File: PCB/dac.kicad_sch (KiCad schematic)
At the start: 8 parts, among them U4 DACx3202

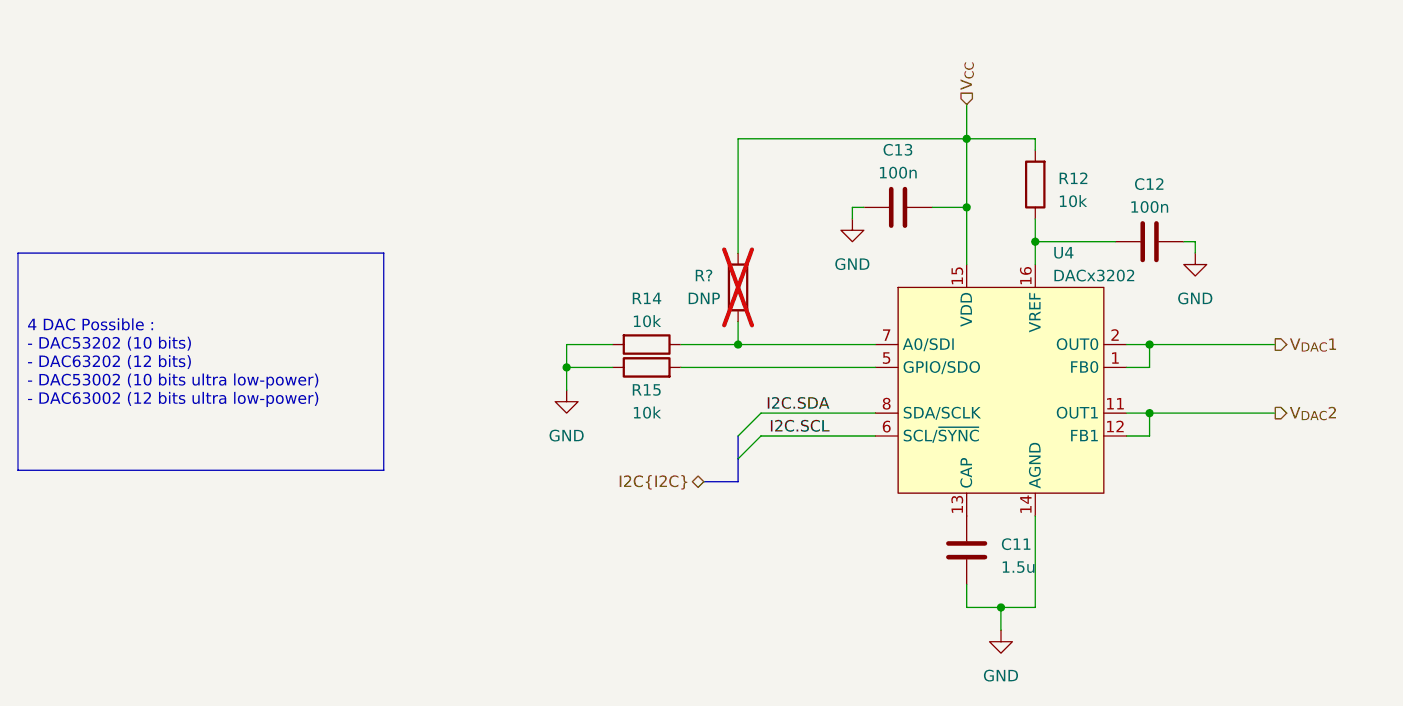
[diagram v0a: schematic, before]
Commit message: done with sch before ERC and footprints
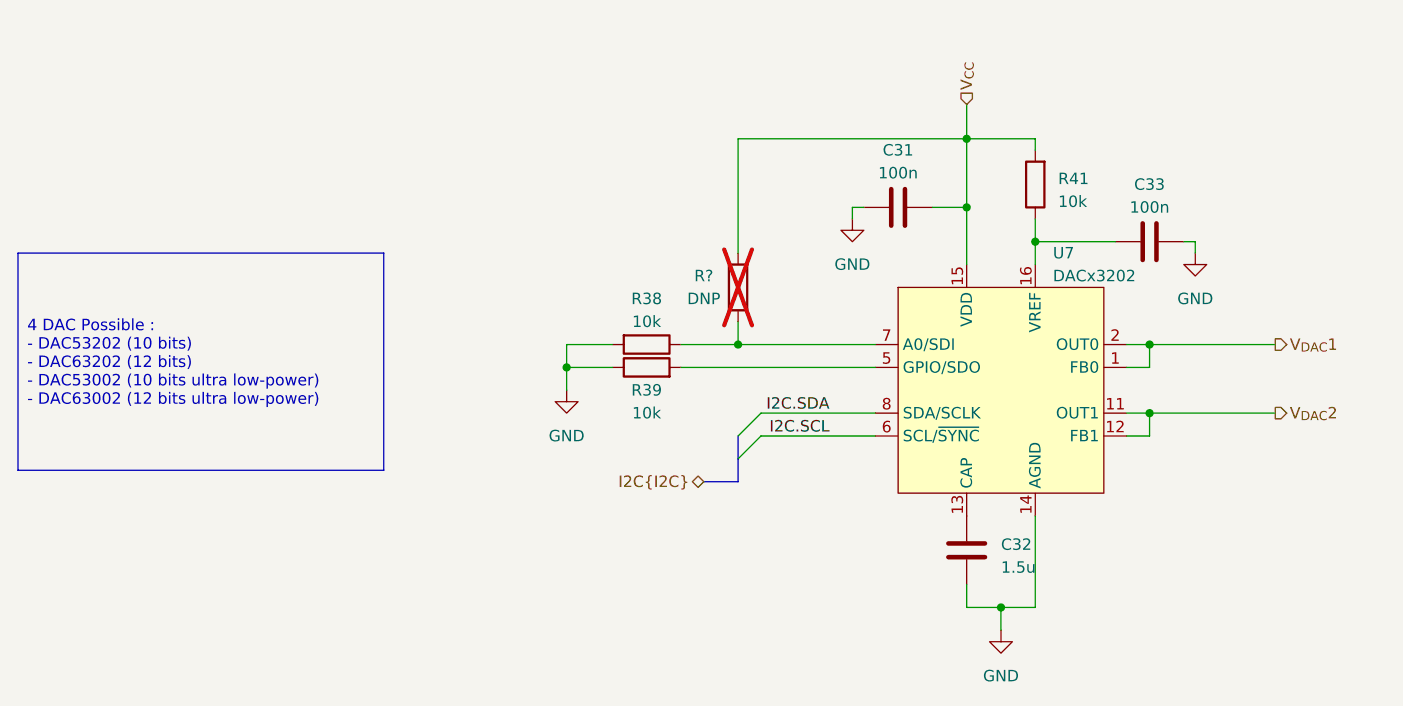
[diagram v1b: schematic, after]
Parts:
- renumbered C13 to C31, C11 to C32, C12 to C33, R14 to R38, R15 to R39, R12 to R41, U4 to U7
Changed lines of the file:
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@@
     (effects (font (size 1.27 1.27)) (justify left))
   )
-  (label "I2C.SCL" (at 134.62 110.49 180)
+  (label "I2C.SCL" (at 134.62 110.49 180) (fields_autoplaced)
     (effects (font (size 1.27 1.27)) (justify right bottom))
   )
-  (label "I2C.SDA" (at 134.62 107.95 180)
+  (label "I2C.SDA" (at 134.62 107.95 180) (fields_autoplaced)
     (effects (font (size 1.27 1.27)) (justify right bottom))
   )
@@
   (symbol (lib_id "power:GND") (at 137.16 86.36 0) (unit 1)
     (in_bom yes) (on_board yes) (dnp no) (fields_autoplaced)
-    (property "Reference" "#PWR031" (at 137.16 92.71 0)
+    (property "Reference" "#PWR065" (at 137.16 92.71 0)
       (effects (font (size 1.27 1.27)) hide)
     )
@@
       (project "Tattoo_Supply"
         (path "/036b57f3-323c-4da7-bad2-1c27fa1415e1/9f555ace-da32-4118-b59a-cfcb78baf4ed"
-          (reference "#PWR031") (unit 1)
+          (reference "#PWR065") (unit 1)
         )
       )
@@
   (symbol (lib_id "Device:R") (at 114.3 102.87 90) (unit 1)
     (in_bom yes) (on_board yes) (dnp no)
-    (property "Reference" "R15" (at 114.3 105.41 90)
+    (property "Reference" "R39" (at 114.3 105.41 90)
       (effects (font (size 1.27 1.27)))
     )
@@
       (project "Tattoo_Supply"
         (path "/036b57f3-323c-4da7-bad2-1c27fa1415e1/9f555ace-da32-4118-b59a-cfcb78baf4ed"
-          (reference "R15") (unit 1)
+          (reference "R39") (unit 1)
         )
       )
@@
         )
         (path "/036b57f3-323c-4da7-bad2-1c27fa1415e1/9f555ace-da32-4118-b59a-cfcb78baf4ed"
-          (reference "R13") (unit 1)
+          (reference "R40") (unit 1)
         )
       )
@@
   (symbol (lib_id "Device:R") (at 114.3 100.33 270) (unit 1)
     (in_bom yes) (on_board yes) (dnp no) (fields_autoplaced)
-    (property "Reference" "R14" (at 114.3 95.25 90)
+    (property "Reference" "R38" (at 114.3 95.25 90)
       (effects (font (size 1.27 1.27)))
     )
@@
       (project "Tattoo_Supply"
         (path "/036b57f3-323c-4da7-bad2-1c27fa1415e1/9f555ace-da32-4118-b59a-cfcb78baf4ed"
-          (reference "R14") (unit 1)
+          (reference "R38") (unit 1)
         )
       )
@@
   (symbol (lib_id "Device:C") (at 142.24 85.09 90) (unit 1)
     (in_bom yes) (on_board yes) (dnp no) (fields_autoplaced)
-    (property "Reference" "C13" (at 142.24 78.74 90)
+    (property "Reference" "C31" (at 142.24 78.74 90)
       (effects (font (size 1.27 1.27)))
     )
@@
       (project "Tattoo_Supply"
         (path "/036b57f3-323c-4da7-bad2-1c27fa1415e1/9f555ace-da32-4118-b59a-cfcb78baf4ed"
-          (reference "C13") (unit 1)
+          (reference "C31") (unit 1)
         )
       )
@@
   (symbol (lib_id "power:GND") (at 105.41 105.41 0) (unit 1)
     (in_bom yes) (on_board yes) (dnp no) (fields_autoplaced)
-    (property "Reference" "#PWR032" (at 105.41 111.76 0)
+    (property "Reference" "#PWR064" (at 105.41 111.76 0)
       (effects (font (size 1.27 1.27)) hide)
     )
@@
       (project "Tattoo_Supply"
         (path "/036b57f3-323c-4da7-bad2-1c27fa1415e1/9f555ace-da32-4118-b59a-cfcb78baf4ed"
-          (reference "#PWR032") (unit 1)
+          (reference "#PWR064") (unit 1)
         )
       )
@@
   (symbol (lib_id "Device:C") (at 149.86 123.19 0) (unit 1)
     (in_bom yes) (on_board yes) (dnp no) (fields_autoplaced)
-    (property "Reference" "C11" (at 153.67 122.555 0)
+    (property "Reference" "C32" (at 153.67 122.555 0)
       (effects (font (size 1.27 1.27)) (justify left))
     )
@@
       (project "Tattoo_Supply"
         (path "/036b57f3-323c-4da7-bad2-1c27fa1415e1/9f555ace-da32-4118-b59a-cfcb78baf4ed"
-          (reference "C11") (unit 1)
+          (reference "C32") (unit 1)
         )
       )
@@
   (symbol (lib_id "power:GND") (at 175.26 90.17 0) (unit 1)
     (in_bom yes) (on_board yes) (dnp no) (fields_autoplaced)
-    (property "Reference" "#PWR030" (at 175.26 96.52 0)
+    (property "Reference" "#PWR067" (at 175.26 96.52 0)
       (effects (font (size 1.27 1.27)) hide)
     )
@@
       (project "Tattoo_Supply"
         (path "/036b57f3-323c-4da7-bad2-1c27fa1415e1/9f555ace-da32-4118-b59a-cfcb78baf4ed"
-          (reference "#PWR030") (unit 1)
+          (reference "#PWR067") (unit 1)
         )
       )
@@
   (symbol (lib_id "Device:R") (at 157.48 82.55 180) (unit 1)
     (in_bom yes) (on_board yes) (dnp no) (fields_autoplaced)
-    (property "Reference" "R12" (at 160.02 81.915 0)
+    (property "Reference" "R41" (at 160.02 81.915 0)
       (effects (font (size 1.27 1.27)) (justify right))
     )
@@
       (project "Tattoo_Supply"
         (path "/036b57f3-323c-4da7-bad2-1c27fa1415e1/9f555ace-da32-4118-b59a-cfcb78baf4ed"
-          (reference "R12") (unit 1)
+          (reference "R41") (unit 1)
         )
       )
@@
   (symbol (lib_id "TattooSupplyLib:DACx3202") (at 153.67 105.41 0) (unit 1)
     (in_bom yes) (on_board yes) (dnp no) (fields_autoplaced)
-    (property "Reference" "U4" (at 159.4359 90.17 0)
+    (property "Reference" "U7" (at 159.4359 90.17 0)
       (effects (font (size 1.27 1.27)) (justify left))
     )
@@
       (project "Tattoo_Supply"
         (path "/036b57f3-323c-4da7-bad2-1c27fa1415e1/9f555ace-da32-4118-b59a-cfcb78baf4ed"
-          (reference "U4") (unit 1)
+          (reference "U7") (unit 1)
         )
       )
@@
   (symbol (lib_id "power:GND") (at 153.67 132.08 0) (unit 1)
     (in_bom yes) (on_board yes) (dnp no) (fields_autoplaced)
-    (property "Reference" "#PWR029" (at 153.67 138.43 0)
+    (property "Reference" "#PWR066" (at 153.67 138.43 0)
       (effects (font (size 1.27 1.27)) hide)
     )
@@
       (project "Tattoo_Supply"
         (path "/036b57f3-323c-4da7-bad2-1c27fa1415e1/9f555ace-da32-4118-b59a-cfcb78baf4ed"
-          (reference "#PWR029") (unit 1)
+          (reference "#PWR066") (unit 1)
         )
       )
@@
   (symbol (lib_id "Device:C") (at 170.18 88.9 90) (unit 1)
     (in_bom yes) (on_board yes) (dnp no) (fields_autoplaced)
-    (property "Reference" "C12" (at 170.18 82.55 90)
+    (property "Reference" "C33" (at 170.18 82.55 90)
       (effects (font (size 1.27 1.27)))
     )
@@
       (project "Tattoo_Supply"
         (path "/036b57f3-323c-4da7-bad2-1c27fa1415e1/9f555ace-da32-4118-b59a-cfcb78baf4ed"
-          (reference "C12") (unit 1)
-        )
-      )
+          (reference "C33") (unit 1)
+        )
+      )

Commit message: begin BOM
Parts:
- C31, C33: footprint (none) -> Capacitor_SMD:C_0603_1608Metric; MPN (none) -> CGA3E2X7R1H104M080AA; Manufacturer (none) -> TDK
- C32: footprint (none) -> Capacitor_SMD:C_0603_1608Metric; MPN (none) -> C1608X7R1A155K080AC; Manufacturer (none) -> TDK
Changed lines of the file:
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@@
+      (effects (font (size 1.27 1.27)) hide)
+    )
+    (property "MPN" "" (at 114.3 102.87 0)
+      (effects (font (size 1.27 1.27)) hide)
+    )
+    (property "Manufacturer" "" (at 114.3 102.87 0)
       (effects (font (size 1.27 1.27)) hide)
     )
@@
       (effects (font (size 1.27 1.27)) hide)
     )
+    (property "MPN" "" (at 124.46 93.98 0)
+      (effects (font (size 1.27 1.27)) hide)
+    )
+    (property "Manufacturer" "" (at 124.46 93.98 0)
+      (effects (font (size 1.27 1.27)) hide)
+    )
     (pin "1")
     (pin "2")
@@
       (effects (font (size 1.27 1.27)) hide)
     )
+    (property "MPN" "" (at 114.3 100.33 0)
+      (effects (font (size 1.27 1.27)) hide)
+    )
+    (property "Manufacturer" "" (at 114.3 100.33 0)
+      (effects (font (size 1.27 1.27)) hide)
+    )
     (pin "1")
     (pin "2")
@@
       (effects (font (size 1.27 1.27)))
     )
-    (property "Footprint" "" (at 146.05 84.1248 0)
+    (property "Footprint" "Capacitor_SMD:C_0603_1608Metric" (at 146.05 84.1248 0)
       (effects (font (size 1.27 1.27)) hide)
     )
     (property "Datasheet" "~" (at 142.24 85.09 0)
+      (effects (font (size 1.27 1.27)) hide)
+    )
+    (property "MPN" "CGA3E2X7R1H104M080AA " (at 142.24 85.09 0)
+      (effects (font (size 1.27 1.27)) hide)
+    )
+    (property "Manufacturer" "TDK" (at 142.24 85.09 0)
       (effects (font (size 1.27 1.27)) hide)
     )
@@
       (effects (font (size 1.27 1.27)) (justify left))
     )
-    (property "Footprint" "" (at 150.8252 127 0)
+    (property "Footprint" "Capacitor_SMD:C_0603_1608Metric" (at 150.8252 127 0)
       (effects (font (size 1.27 1.27)) hide)
     )
     (property "Datasheet" "~" (at 149.86 123.19 0)
+      (effects (font (size 1.27 1.27)) hide)
+    )
+    (property "MPN" "C1608X7R1A155K080AC" (at 149.86 123.19 0)
+      (effects (font (size 1.27 1.27)) hide)
+    )
+    (property "Manufacturer" "TDK" (at 149.86 123.19 0)
       (effects (font (size 1.27 1.27)) hide)
     )
@@
       (effects (font (size 1.27 1.27)) hide)
     )
+    (property "MPN" "" (at 157.48 82.55 0)
+      (effects (font (size 1.27 1.27)) hide)
+    )
+    (property "Manufacturer" "" (at 157.48 82.55 0)
+      (effects (font (size 1.27 1.27)) hide)
+    )
     (pin "1")
     (pin "2")
@@
     )
     (property "Datasheet" "" (at 153.67 76.2 0)
+      (effects (font (size 1.27 1.27)) hide)
+    )
+    (property "MPN" "" (at 153.67 105.41 0)
+      (effects (font (size 1.27 1.27)) hide)
+    )
+    (property "Manufacturer" "" (at 153.67 105.41 0)
       (effects (font (size 1.27 1.27)) hide)
     )
@@
       (effects (font (size 1.27 1.27)))
     )
-    (property "Footprint" "" (at 173.99 87.9348 0)
+    (property "Footprint" "Capacitor_SMD:C_0603_1608Metric" (at 173.99 87.9348 0)
       (effects (font (size 1.27 1.27)) hide)
     )
@@
       (effects (font (size 1.27 1.27)) hide)
     )
+    (property "MPN" "CGA3E2X7R1H104M080AA " (at 170.18 88.9 0)
+      (effects (font (size 1.27 1.27)) hide)
+    )
+    (property "Manufacturer" "TDK" (at 170.18 88.9 0)
+      (effects (font (size 1.27 1.27)) hide)
+    )

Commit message: Resistors ok in BOM
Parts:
- R38, R39, R41: footprint (none) -> Resistor_SMD:R_0603_1608Metric; MPN (none) -> ERJ-3EKF1002V; Manufacturer (none) -> Panasonic
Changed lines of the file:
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@@
       (effects (font (size 1.27 1.27)))
     )
-    (property "Footprint" "" (at 114.3 104.648 90)
+    (property "Footprint" "Resistor_SMD:R_0603_1608Metric" (at 114.3 104.648 90)
       (effects (font (size 1.27 1.27)) hide)
     )
@@
       (effects (font (size 1.27 1.27)) hide)
     )
-    (property "MPN" "" (at 114.3 102.87 0)
-      (effects (font (size 1.27 1.27)) hide)
-    )
-    (property "Manufacturer" "" (at 114.3 102.87 0)
+    (property "MPN" "ERJ-3EKF1002V" (at 114.3 102.87 0)
+      (effects (font (size 1.27 1.27)) hide)
+    )
+    (property "Manufacturer" "Panasonic" (at 114.3 102.87 0)
       (effects (font (size 1.27 1.27)) hide)
     )
@@
       (effects (font (size 1.27 1.27)))
     )
-    (property "Footprint" "" (at 114.3 98.552 90)
+    (property "Footprint" "Resistor_SMD:R_0603_1608Metric" (at 114.3 98.552 90)
       (effects (font (size 1.27 1.27)) hide)
     )
@@
       (effects (font (size 1.27 1.27)) hide)
     )
-    (property "MPN" "" (at 114.3 100.33 0)
-      (effects (font (size 1.27 1.27)) hide)
-    )
-    (property "Manufacturer" "" (at 114.3 100.33 0)
+    (property "MPN" "ERJ-3EKF1002V" (at 114.3 100.33 0)
+      (effects (font (size 1.27 1.27)) hide)
+    )
+    (property "Manufacturer" "Panasonic" (at 114.3 100.33 0)
       (effects (font (size 1.27 1.27)) hide)
     )
@@
       (effects (font (size 1.27 1.27)) (justify right))
     )
-    (property "Footprint" "" (at 159.258 82.55 90)
+    (property "Footprint" "Resistor_SMD:R_0603_1608Metric" (at 159.258 82.55 90)
       (effects (font (size 1.27 1.27)) hide)
     )
@@
       (effects (font (size 1.27 1.27)) hide)
     )
-    (property "MPN" "" (at 157.48 82.55 0)
-      (effects (font (size 1.27 1.27)) hide)
-    )
-    (property "Manufacturer" "" (at 157.48 82.55 0)
-      (effects (font (size 1.27 1.27)) hide)
-    )
+    (property "MPN" "ERJ-3EKF1002V" (at 157.48 82.55 0)
+      (effects (font (size 1.27 1.27)) hide)
+    )
+    (property "Manufacturer" "Panasonic" (at 157.48 82.55 0)
+      (effects (font (size 1.27 1.27)) hide)
+    )

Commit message: bom almost finished
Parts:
- U7: MPN (none) -> DAC63202RTER; Manufacturer (none) -> Texas Instruments
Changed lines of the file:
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@@
       (effects (font (size 1.27 1.27)) hide)
     )
-    (property "MPN" "" (at 153.67 105.41 0)
+    (property "MPN" "DAC63202RTER" (at 153.67 105.41 0)
       (effects (font (size 1.27 1.27)) hide)
     )
-    (property "Manufacturer" "" (at 153.67 105.41 0)
+    (property "Manufacturer" "Texas Instruments" (at 153.67 105.41 0)
       (effects (font (size 1.27 1.27)) hide)
     )

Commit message: add 3d models
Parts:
- R?: footprint (none) -> Resistor_SMD:R_0603_1608Metric
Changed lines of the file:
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@@
       (effects (font (size 1.27 1.27)))
     )
-    (property "Footprint" "" (at 126.238 93.98 90)
+    (property "Footprint" "Resistor_SMD:R_0603_1608Metric" (at 126.238 93.98 90)
       (effects (font (size 1.27 1.27)) hide)
     )

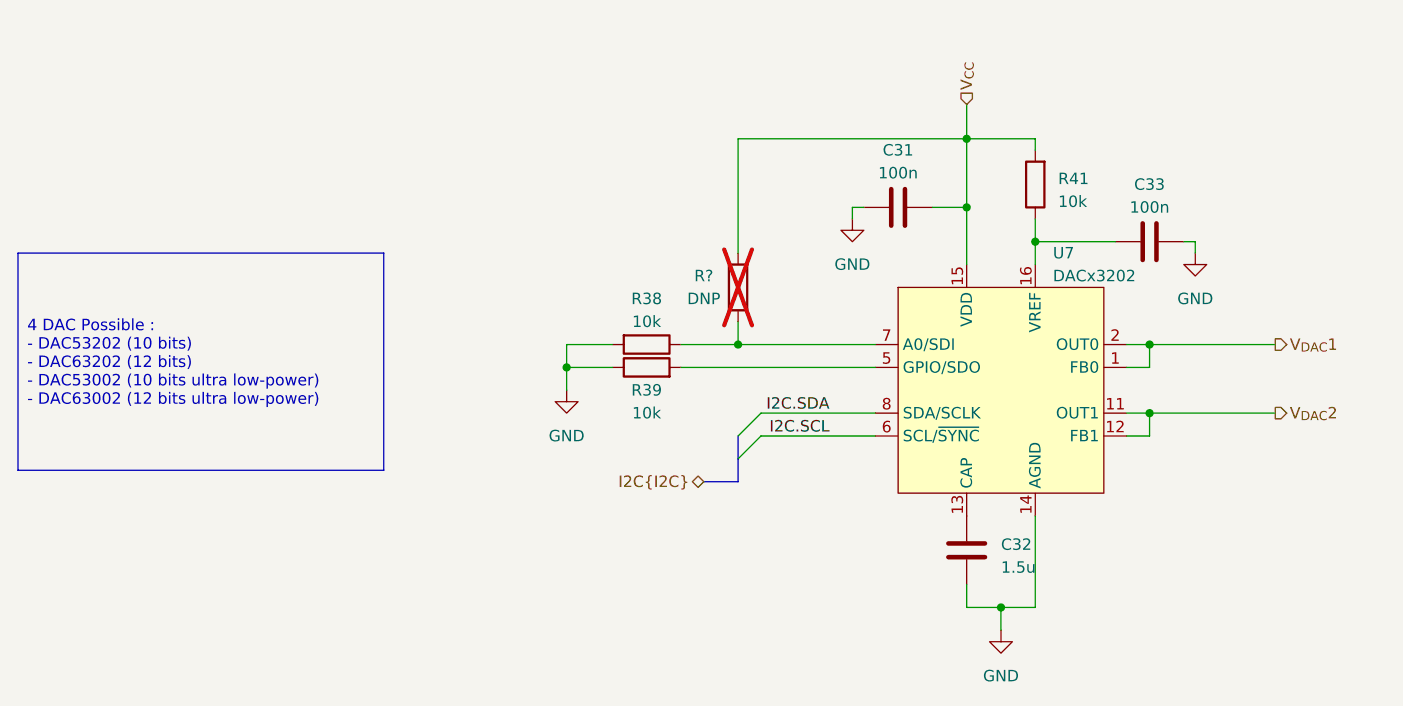
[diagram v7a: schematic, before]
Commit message: switch kicad 8 and change USB connector
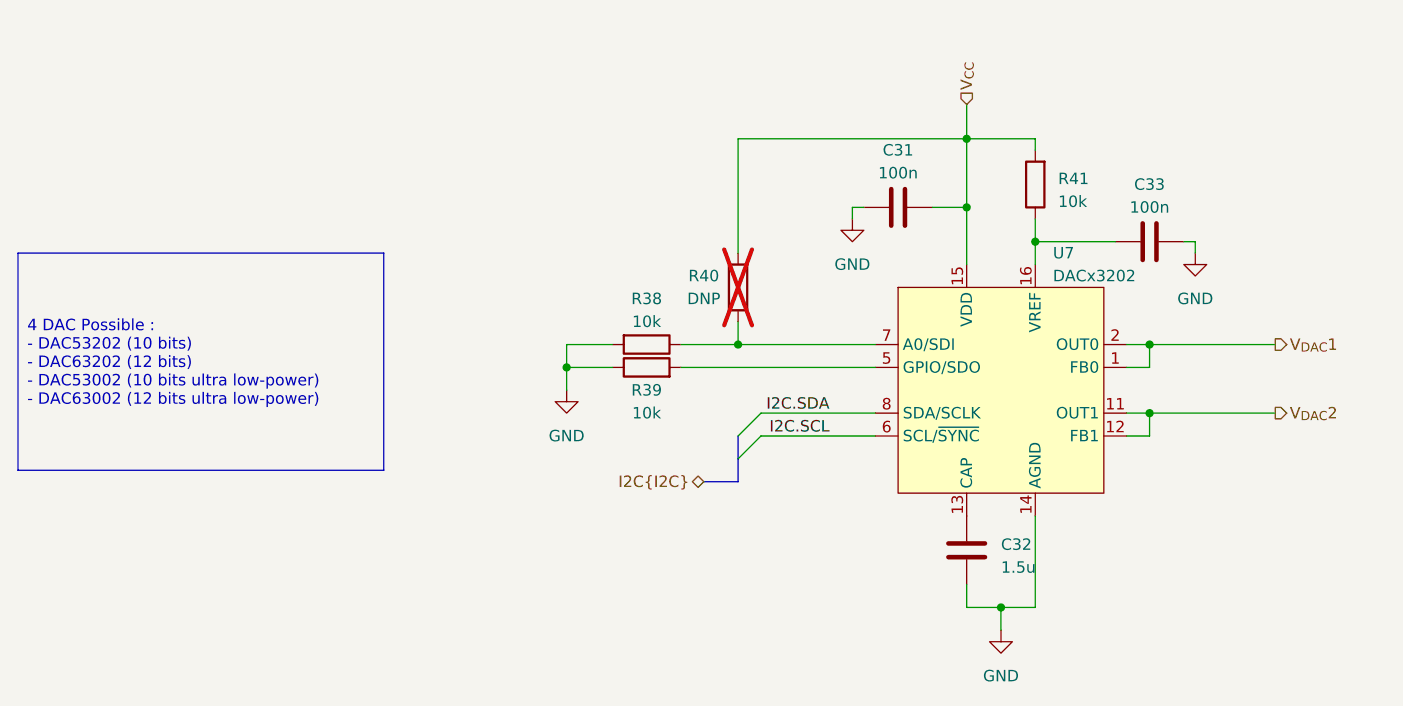
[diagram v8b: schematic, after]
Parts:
- gave numbers to parts that had none: 1
